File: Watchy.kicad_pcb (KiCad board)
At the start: 4 copper layers, 33.8 x 46 mm, 75 parts, among them J1 FPC24(0.5MM), J2 USB_C_Receptacle_USB2.0, J3 Conn_01x01, J4 Conn_01x01, M1 Vibration_Motor, Q1 AO3400A, Q2 S8050, Q3 CJ2301, SW1 BTN, SW2 BTN, SW3 BTN, SW4 BTN, U2 TP4054, U3 BMA423, U4 ME6211C33M5G-N

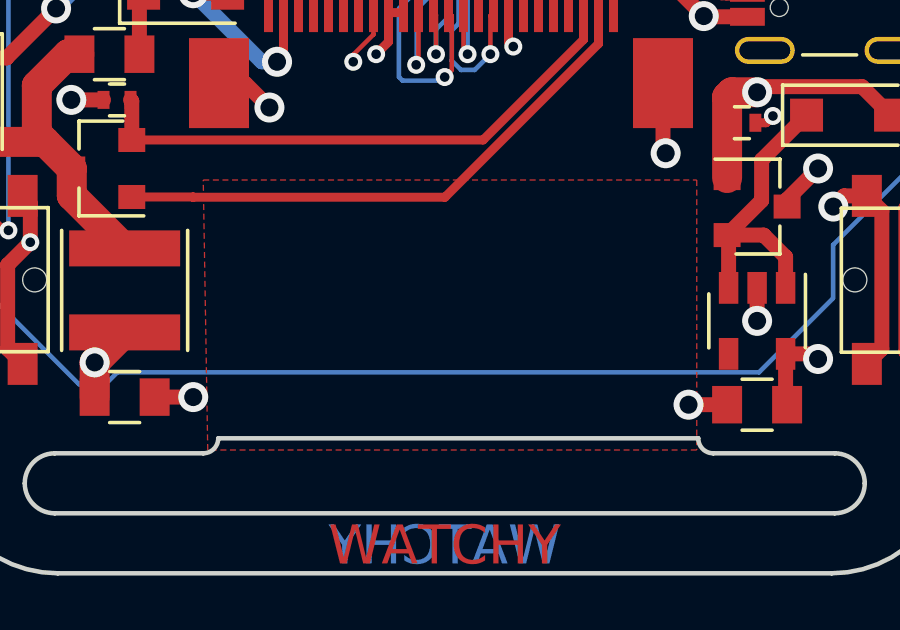
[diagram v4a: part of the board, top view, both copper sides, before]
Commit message: Removed zone under logos
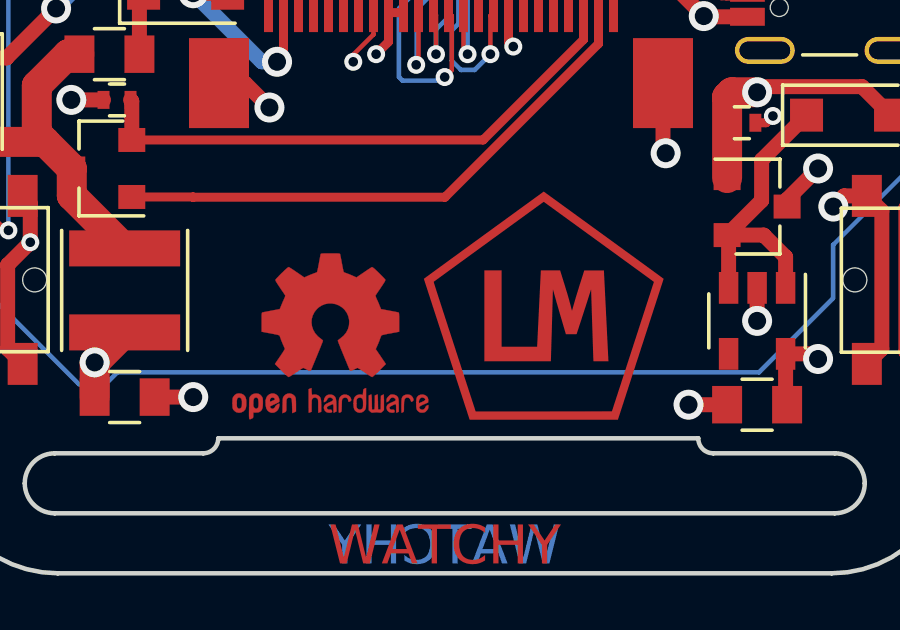
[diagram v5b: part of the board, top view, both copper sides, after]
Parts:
- added A1: ~, Watchy:logoLM, F.Cu at (88.9, 107.2)
- added REF**: OSHW-Logo2_7.3x6mm_SilkScreen, Symbol:OSHW-Logo2_7.3x6mm_SilkScreen, F.Cu at (81.8, 108.2)
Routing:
- removed copper zone on F.Cu, net (none)
